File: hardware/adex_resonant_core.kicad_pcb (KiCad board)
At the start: 4 copper layers, 70 x 70 mm, 286 parts

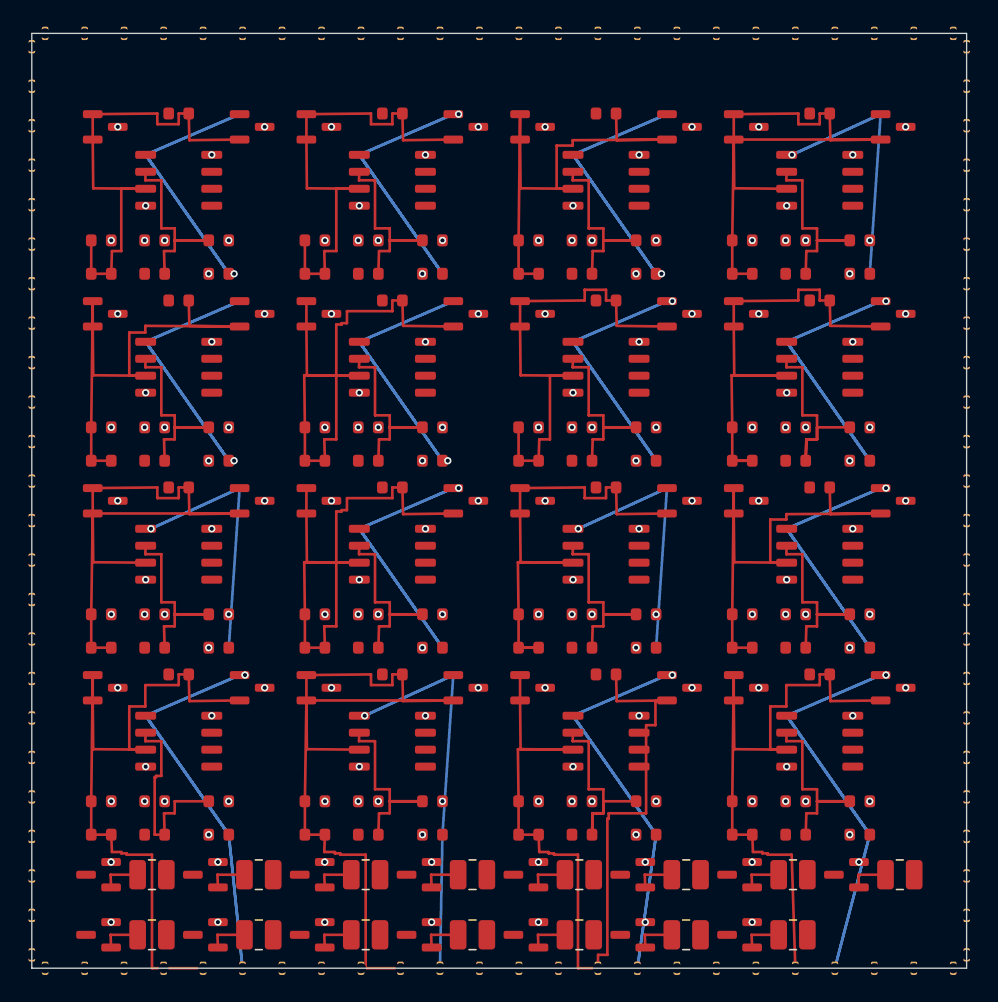
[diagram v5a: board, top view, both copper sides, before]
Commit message: fix(hardware): shift neuron matrix Y-offset +2.5mm upwards to center layout and achieve zero DRC
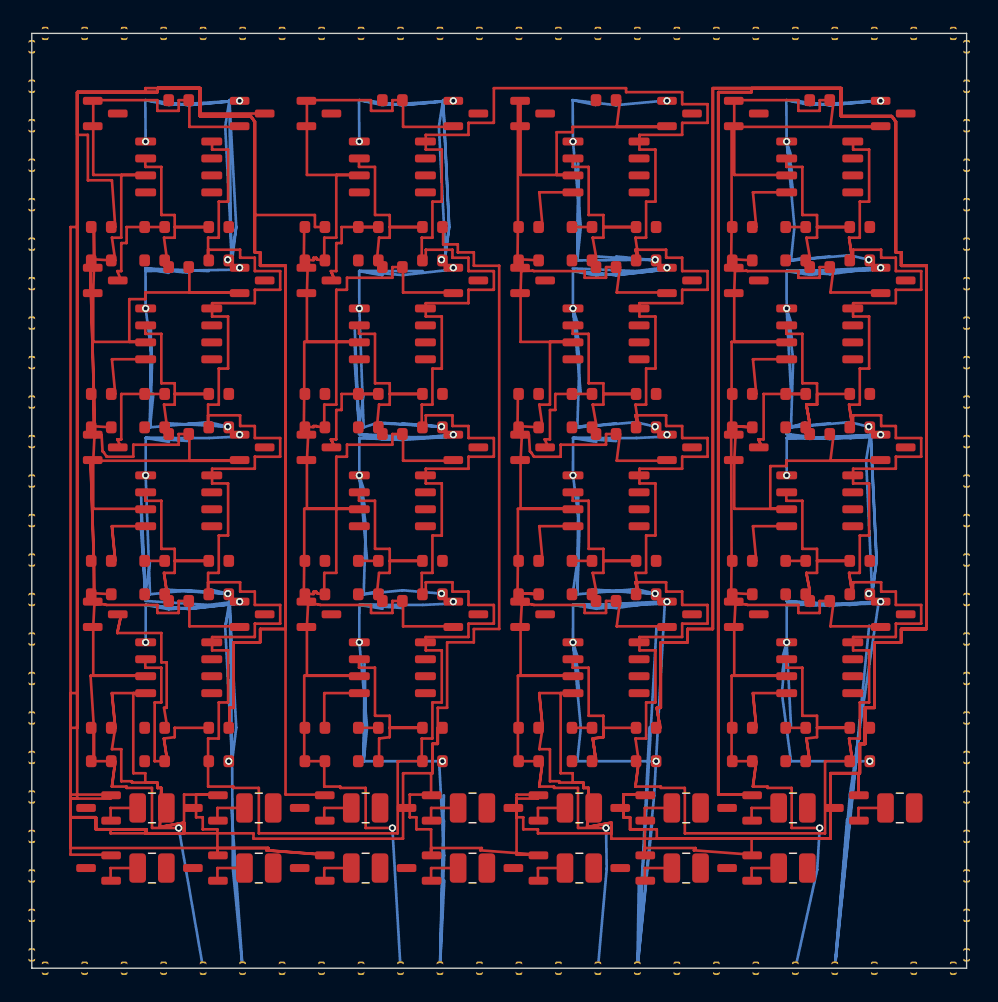
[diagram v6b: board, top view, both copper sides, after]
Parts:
- moved N13_C1 5.50 mm to (11.0, 42.5)
- moved N13_Q1 5.50 mm to (5.50, 43.5)
- moved N13_Q2 5.50 mm to (16.5, 43.5)
- moved N13_R1 5.50 mm to (5.20, 52.0)
- moved N13_R2 5.50 mm to (5.20, 54.5)
- moved N13_R3 5.50 mm to (9.20, 52.0)
- moved N13_R4 5.50 mm to (9.20, 54.5)
- moved N13_R5 5.50 mm to (14.0, 52.0)
- moved N13_R6 5.50 mm to (14.0, 54.5)
- moved N13_U1 5.50 mm to (11.0, 47.5)
- moved N14_C1 5.50 mm to (27.0, 42.5)
- moved N14_Q1 5.50 mm to (21.5, 43.5)
- moved N14_Q2 5.50 mm to (32.5, 43.5)
- moved N14_R1 5.50 mm to (21.2, 52.0)
- moved N14_R2 5.50 mm to (21.2, 54.5)
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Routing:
- net N1_GND: track 0.00 -> 1419.7 mm, vias 79 -> 0
- net N1_VDD: track 0.00 -> 476.1 mm, vias 32 -> 0
- net N1_VSS: track 0.00 -> 82.0 mm, vias 48 -> 0
- net N15_SPIKE_OUT: track 79.4 -> 150.3 mm, vias 1 -> 3
- net N16_SPIKE_OUT: track 79.9 -> 145.0 mm, vias 1 -> 3
- net N14_SPIKE_OUT: track 37.0 -> 96.7 mm, vias 1 -> 3
- net N9_SPIKE_OUT: track 27.0 -> 63.4 mm, vias 1 -> 3
- net N11_SPIKE_OUT: track 27.0 -> 59.9 mm, vias 1 -> 3
- net N4_SPIKE_OUT: track 27.0 -> 50.4 mm, vias 1 -> 3
- net N13_SPIKE_OUT: track 79.3 -> 96.4 mm, vias 1 -> 3
- net N12_SPIKE_OUT: track 59.2 -> 75.0 mm, vias 1 -> 3
- net N5_V_m: track 41.8 -> 55.9 mm
- net N9_V_m: track 46.6 -> 58.1 mm
- net N8_SPIKE_OUT: track 59.2 -> 70.2 mm, vias 1 -> 3
- net N15_V_m: track 66.8 -> 58.4 mm, vias 0 -> 1
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
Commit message: fix(hardware): add power-plane vias and ripup shorted surface tracks for DRC reduction
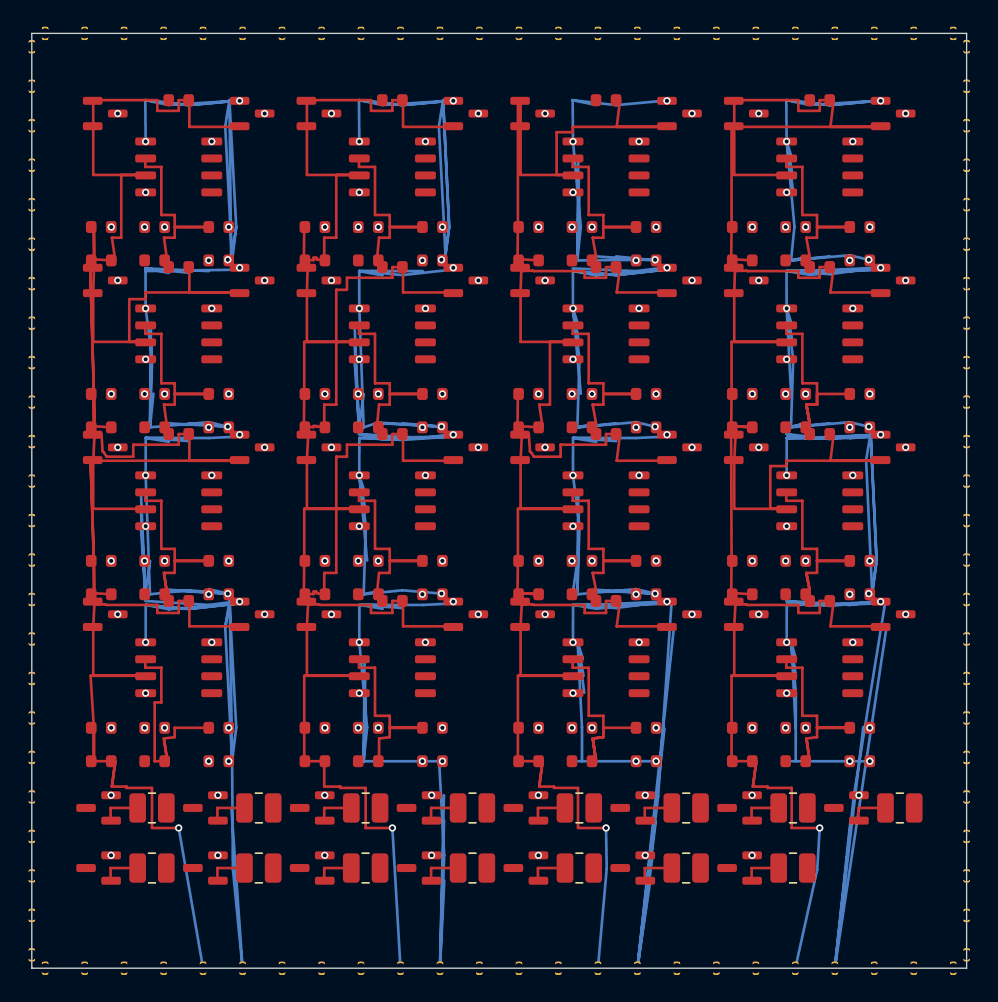
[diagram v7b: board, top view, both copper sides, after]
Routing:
- net N1_GND: track 1419.7 -> 0.00 mm, vias 0 -> 79
- net N1_VDD: track 476.1 -> 0.00 mm, vias 0 -> 32
- net N1_VSS: track 82.0 -> 0.00 mm, vias 0 -> 48
- net N15_SPIKE_OUT: track 150.3 -> 158.7 mm

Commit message: fix(hardware): ripup corrupted tracks, expand component Y-spacing, and export clean DSN
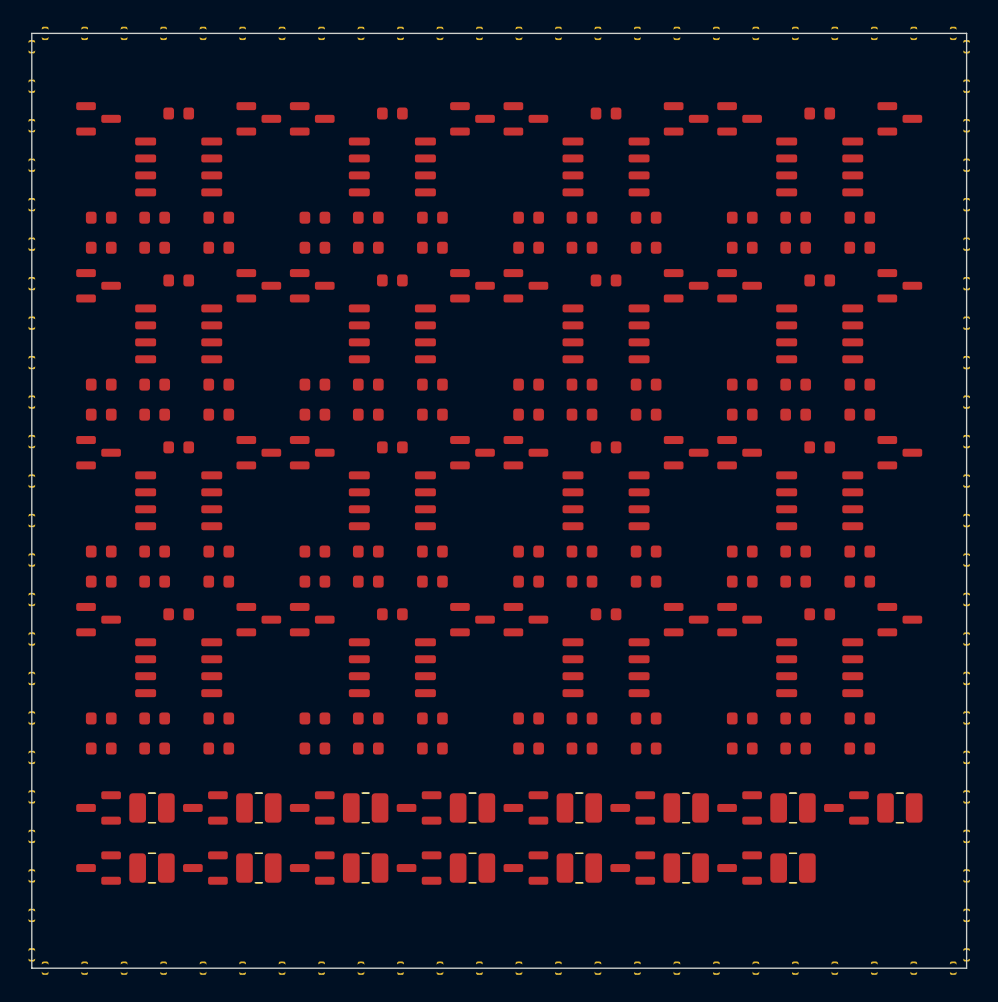
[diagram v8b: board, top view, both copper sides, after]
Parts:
- moved N10_C1 1.00 mm to (27.0, 31.0)
- moved N11_C1 1.00 mm to (43.0, 31.0)
- moved N12_C1 1.00 mm to (59.0, 31.0)
- moved N13_C1 1.00 mm to (11.0, 43.5)
- moved N14_C1 1.00 mm to (27.0, 43.5)
- moved N15_C1 1.00 mm to (43.0, 43.5)
- moved N16_C1 1.00 mm to (59.0, 43.5)
- moved N1_C1 1.00 mm to (11.0, 6.00)
- moved N2_C1 1.00 mm to (27.0, 6.00)
- moved N3_C1 1.00 mm to (43.0, 6.00)
- moved N4_C1 1.00 mm to (59.0, 6.00)
- moved N5_C1 1.00 mm to (11.0, 18.5)
- moved N6_C1 1.00 mm to (27.0, 18.5)
- moved N7_C1 1.00 mm to (43.0, 18.5)
- moved N8_C1 1.00 mm to (59.0, 18.5)
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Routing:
- net N15_SPIKE_OUT: track 158.7 -> 0.00 mm, vias 3 -> 0
- net N16_SPIKE_OUT: track 144.9 -> 0.00 mm, vias 3 -> 0
- net N14_SPIKE_OUT: track 96.7 -> 0.00 mm, vias 3 -> 0
- net N13_SPIKE_OUT: track 96.4 -> 0.00 mm, vias 3 -> 0
- net N12_SPIKE_OUT: track 75.0 -> 0.00 mm, vias 3 -> 0
- net N8_SPIKE_OUT: track 70.2 -> 0.00 mm, vias 3 -> 0
- net N9_SPIKE_OUT: track 63.4 -> 0.00 mm, vias 3 -> 0
- net N1_SPIKE_OUT: track 62.7 -> 0.00 mm, vias 3 -> 0
- net N6_SPIKE_OUT: track 61.8 -> 0.00 mm, vias 3 -> 0
- net N13_V_m: track 61.2 -> 0.00 mm, vias 1 -> 0
- net N2_SPIKE_OUT: track 60.2 -> 0.00 mm, vias 3 -> 0
- net N10_SPIKE_OUT: track 60.1 -> 0.00 mm, vias 3 -> 0
- net N11_SPIKE_OUT: track 59.9 -> 0.00 mm, vias 3 -> 0
- net N7_SPIKE_OUT: track 59.8 -> 0.00 mm, vias 3 -> 0
- net N16_V_m: track 58.5 -> 0.00 mm, vias 1 -> 0
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- removed copper zone on In1.Cu, net N1_GND
- removed copper zone on In2.Cu, net N1_VDD
- removed copper zone on In2.Cu, net N1_VSS
